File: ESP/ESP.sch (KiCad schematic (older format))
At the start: 28 parts, among them J3 USB_B_Micro, J4 Micro_SD_Card_Det, Q1 mmbt2222, Q2 mmbt2222, U1 ESP32-PICO-D4, U2 AP2112K-3.3, U3 CP2104

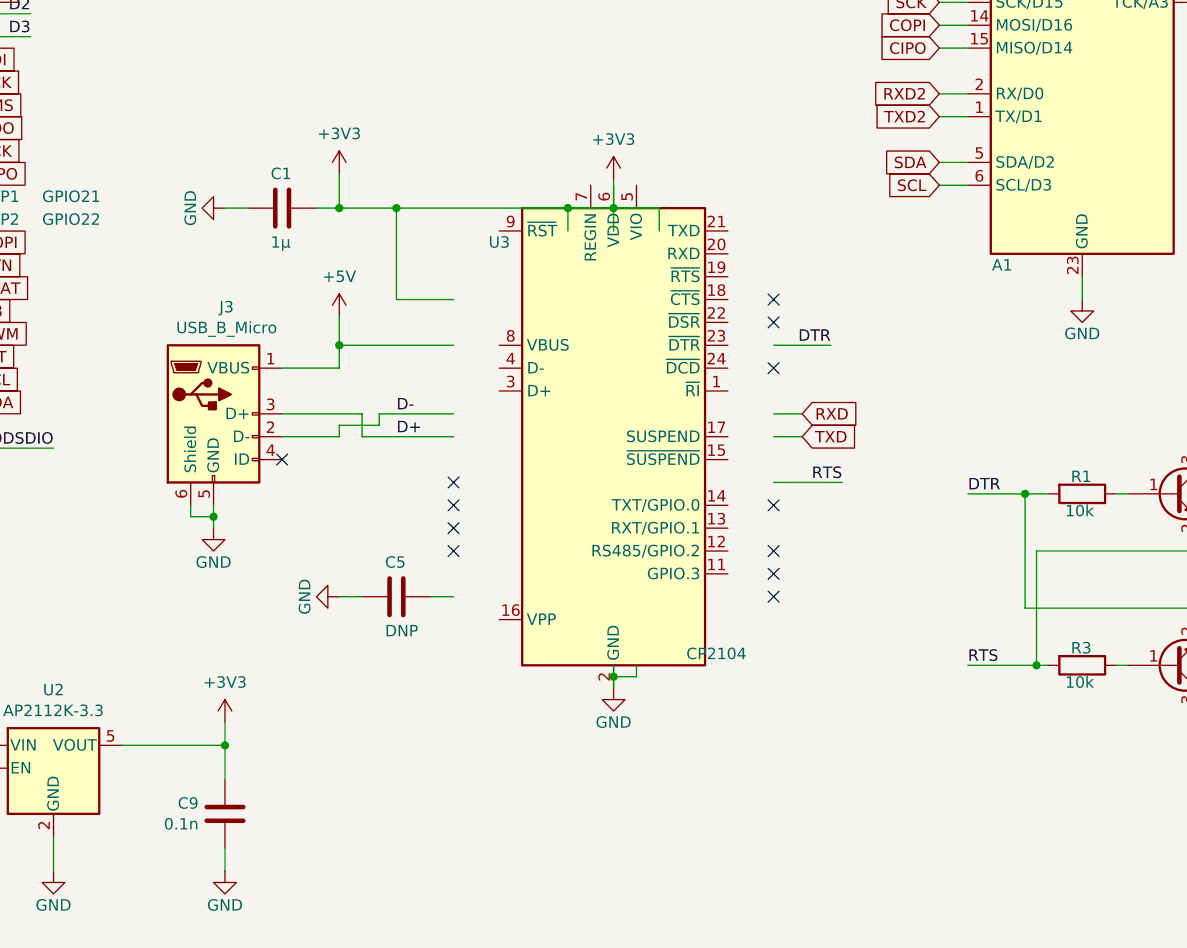
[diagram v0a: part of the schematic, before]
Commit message: changed VCC of CP2104
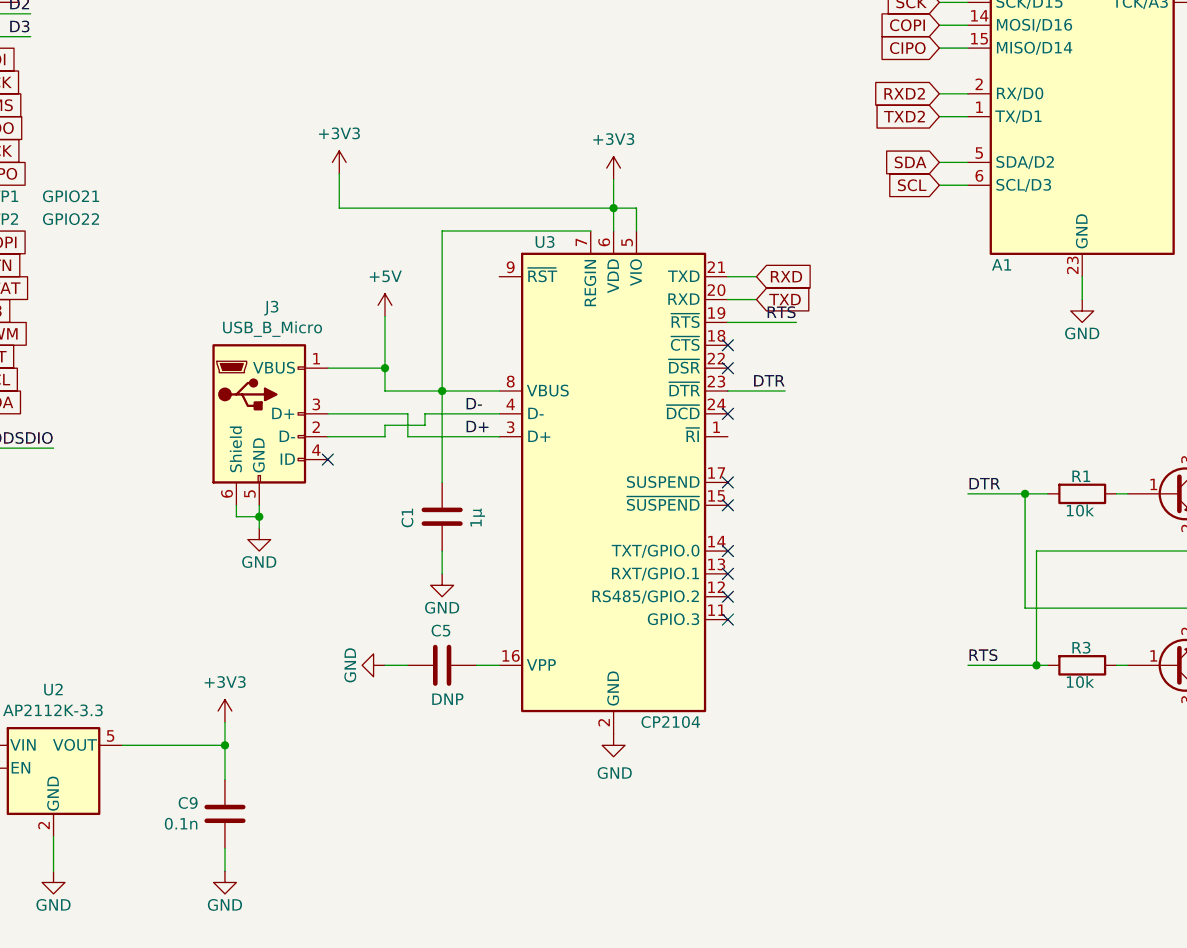
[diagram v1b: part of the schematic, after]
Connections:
- wire segments 160 -> 154
- no-connect marks 20 -> 18
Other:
- moved on the sheet: C1, C5, J3, U3
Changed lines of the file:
@@
 Sheet 1 1
 Title "ProMicro_ESP"
-Date "2021-04-19"
-Rev "v1.0"
+Date "2021-04-20"
+Rev "v1.1"
 Comp "nerdyscout"
 Comment1 ""
@@
 	9550 6000 9550 5500
 Connection ~ 9550 6000
-Wire Wire Line
-	9500 5250 9250 5250
 Connection ~ 9500 5250
 Wire Wire Line
@@
 $EndComp
 $Comp
-L power:GND #PWR0113
-U 1 1 60528891
-P 7700 6100
-F 0 "#PWR0113" H 7700 5850 50  0001 C CNN
-F 1 "GND" H 7700 5950 50  0000 C CNN
-F 2 "" H 7700 6100 50  0001 C CNN
-F 3 "" H 7700 6100 50  0001 C CNN
-	1    7700 6100
-	1    0    0    -1
-$EndComp
-Wire Wire Line
-	7700 6100 7700 6050
-Wire Wire Line
-	7700 6050 7800 6050
-Wire Wire Line
-	7800 6050 7800 6000
-Connection ~ 7700 6050
-Wire Wire Line
-	7700 6050 7700 6000
-$Comp
 L power:+3V3 #PWR0114
 U 1 1 60537586
@@
 Wire Wire Line
 	7700 4100 7700 4000
-Wire Wire Line
-	7500 4100 7500 4000
-Wire Wire Line
-	7500 4000 7700 4000
 Connection ~ 7700 4000
 Wire Wire Line
 	7700 4000 7700 3875
-Text GLabel 8525 5000 2    50   Input ~ 0
+Text GLabel 8325 4400 2    50   Input ~ 0
 TXD
-Text GLabel 8525 4900 2    50   Input ~ 0
+Text GLabel 8325 4300 2    50   Input ~ 0
 RXD
-Text Label 8650 4600 2    50   ~ 0
+Text Label 8450 4800 2    50   ~ 0
 DTR
-Text Label 8700 5200 2    50   ~ 0
+Text Label 8500 4500 2    50   ~ 0
 RTS
 Wire Wire Line
-	8400 5200 8700 5200
-Wire Wire Line
-	8400 4600 8650 4600
-Wire Wire Line
-	8525 5000 8400 5000
-Wire Wire Line
-	8400 4900 8525 4900
-NoConn ~ 8400 4400
-NoConn ~ 8400 4500
-NoConn ~ 8400 5300
+	8200 4500 8500 4500
+Wire Wire Line
+	8200 4800 8450 4800
+Wire Wire Line
+	8325 4400 8200 4400
+Wire Wire Line
+	8200 4300 8325 4300
+NoConn ~ 8200 4600
+NoConn ~ 8200 4700
+NoConn ~ 8200 5300
 $Comp
 L Device:C C1
 U 1 1 605A71B6
-P 6250 4000
-F 0 "C1" V 6100 3950 50  0000 L CNN
-F 1 "1µ" V 6400 3950 50  0000 L CNN
-F 2 "Capacitor_SMD:C_0603_1608Metric" H 6288 3850 50  0001 C CNN
-F 3 "~" H 6250 4000 50  0001 C CNN
-	1    6250 4000
-	0    1    1    0
-$EndComp
-Wire Wire Line
-	6400 4000 6500 4000
+P 6950 5350
+F 0 "C1" V 6800 5300 50  0000 L CNN
+F 1 "1µ" V 7100 5300 50  0000 L CNN
+F 2 "Capacitor_SMD:C_0603_1608Metric" H 6988 5200 50  0001 C CNN
+F 3 "~" H 6950 5350 50  0001 C CNN
+	1    6950 5350
+	1    0    0    -1
+$EndComp
 $Comp
 L power:GND #PWR0115
 U 1 1 605A71C1
-P 6000 4000
-F 0 "#PWR0115" H 6000 3750 50  0001 C CNN
-F 1 "GND" H 6000 3850 50  0000 C CNN
-F 2 "" H 6000 4000 50  0001 C CNN
-F 3 "" H 6000 4000 50  0001 C CNN
-	1    6000 4000
-	0    1    1    0
-$EndComp
-Wire Wire Line
-	6000 4000 6100 4000
+P 6950 5600
+F 0 "#PWR0115" H 6950 5350 50  0001 C CNN
+F 1 "GND" H 6950 5450 50  0000 C CNN
+F 2 "" H 6950 5600 50  0001 C CNN
+F 3 "" H 6950 5600 50  0001 C CNN
+	1    6950 5600
+	1    0    0    -1
+$EndComp
+Wire Wire Line
+	6950 5600 6950 5500
 $Comp
 L power:+3V3 #PWR0116
@@
 Wire Wire Line
 	6500 3850 6500 4000
-Connection ~ 6500 4000
-Wire Wire Line
-	6500 4000 6750 4000
-Connection ~ 7500 4000
-Wire Wire Line
-	7000 4400 6750 4400
-Wire Wire Line
-	7900 4100 7900 4000
-Wire Wire Line
-	7700 4000 7900 4000
-Wire Wire Line
-	6250 5000 6500 5000
-Wire Wire Line
-	6500 5000 6500 4950
-Wire Wire Line
-	6500 4950 6675 4950
-Wire Wire Line
-	6675 4950 6675 4900
-Wire Wire Line
-	6675 4900 7000 4900
-Wire Wire Line
-	7000 5000 6600 5000
-Wire Wire Line
-	6600 5000 6600 4900
-Wire Wire Line
-	6600 4900 6250 4900
+Wire Wire Line
+	7700 4000 7800 4000
+Wire Wire Line
+	6450 5000 6700 5000
+Wire Wire Line
+	6700 5000 6700 4950
+Wire Wire Line
+	6700 4950 6875 4950
+Wire Wire Line
+	6875 4950 6875 4900
+Wire Wire Line
+	6875 4900 7200 4900
+Wire Wire Line
+	7200 5000 6800 5000
+Wire Wire Line
+	6800 5000 6800 4900
+Wire Wire Line
+	6800 4900 6450 4900
 $Comp
 L power:GND #PWR0118
 U 1 1 6060CE03
-P 5950 5400
-F 0 "#PWR0118" H 5950 5150 50  0001 C CNN
-F 1 "GND" H 5950 5250 50  0000 C CNN
-F 2 "" H 5950 5400 50  0001 C CNN
-F 3 "" H 5950 5400 50  0001 C CNN
-	1    5950 5400
-	1    0    0    -1
-$EndComp
-Wire Wire Line
-	5950 5400 5950 5350
-Wire Wire Line
-	5950 5350 5850 5350
-Wire Wire Line
-	5850 5350 5850 5300
-Connection ~ 5950 5350
-Wire Wire Line
-	5950 5350 5950 5300
+P 6150 5400
+F 0 "#PWR0118" H 6150 5150 50  0001 C CNN
+F 1 "GND" H 6150 5250 50  0000 C CNN
+F 2 "" H 6150 5400 50  0001 C CNN
+F 3 "" H 6150 5400 50  0001 C CNN
+	1    6150 5400
+	1    0    0    -1
+$EndComp
+Wire Wire Line
+	6150 5400 6150 5350
+Wire Wire Line
+	6150 5350 6050 5350
+Wire Wire Line
+	6050 5350 6050 5300
+Connection ~ 6150 5350
+Wire Wire Line
+	6150 5350 6150 5300
 Text Label 3150 6600 2    50   ~ 0
 CLK
@@
 L power:+5V #PWR0126
 U 1 1 60613DA0
-P 6500 4475
-F 0 "#PWR0126" H 6500 4325 50  0001 C CNN
-F 1 "+5V" H 6500 4650 50  0000 C CNN
-F 2 "" H 6500 4475 50  0001 C CNN
-F 3 "" H 6500 4475 50  0001 C CNN
-	1    6500 4475
-	1    0    0    -1
-$EndComp
-Wire Wire Line
-	7000 4600 6500 4600
-Wire Wire Line
-	6500 4600 6500 4475
-Wire Wire Line
-	6250 4700 6500 4700
-Wire Wire Line
-	6500 4700 6500 4600
-Connection ~ 6500 4600
-Wire Wire Line
-	6750 4400 6750 4000
-Connection ~ 6750 4000
-Wire Wire Line
-	6750 4000 7500 4000
+P 6700 4475
+F 0 "#PWR0126" H 6700 4325 50  0001 C CNN
+F 1 "+5V" H 6700 4650 50  0000 C CNN
+F 2 "" H 6700 4475 50  0001 C CNN
+F 3 "" H 6700 4475 50  0001 C CNN
+	1    6700 4475
+	1    0    0    -1
+$EndComp
+Wire Wire Line
+	6450 4700 6700 4700
 $Comp
 L Regulator_Linear:AP2112K-3.3 U2
@@
 L Connector:USB_B_Micro J3
 U 1 1 6079D873
-P 5950 4900
-F 0 "J3" H 6007 5367 50  0000 C CNN
-F 1 "USB_B_Micro" H 6007 5276 50  0000 C CNN
-F 2 "Connector_USB:USB_Micro-B_Molex_47346-0001" H 6100 4850 50  0001 C CNN
-F 3 "~" H 6100 4850 50  0001 C CNN
-	1    5950 4900
+P 6150 4900
+F 0 "J3" H 6207 5367 50  0000 C CNN
+F 1 "USB_B_Micro" H 6207 5276 50  0000 C CNN
+F 2 "Connector_USB:USB_Micro-B_Molex_47346-0001" H 6300 4850 50  0001 C CNN
+F 3 "~" H 6300 4850 50  0001 C CNN
+	1    6150 4900
 	1    0    0    -1
 $EndComp
@@
 L Interface_USB:CP2104 U3
 U 1 1 604CC18C
-P 7700 5000
-F 0 "U3" H 7200 5850 50  0000 C CNN
-F 1 "CP2104" H 8150 4050 50  0000 C CNN
-F 2 "Package_DFN_QFN:QFN-24-1EP_4x4mm_P0.5mm_EP2.6x2.6mm" H 7850 4050 50  0001 L CNN
-F 3 "https://www.silabs.com/documents/public/data-sheets/cp2104.pdf" H 7150 6250 50  0001 C CNN
-	1    7700 5000
-	1    0    0    -1
-$EndComp
-Wire Wire Line
-	6900 5700 7000 5700
+P 7700 5200
+F 0 "U3" H 7400 6250 50  0000 C CNN
+F 1 "CP2104" H 7950 4150 50  0000 C CNN
+F 2 "Package_DFN_QFN:QFN-24-1EP_4x4mm_P0.5mm_EP2.6x2.6mm" H 7850 4250 50  0001 L CNN
+F 3 "https://www.silabs.com/documents/public/data-sheets/cp2104.pdf" H 7150 6450 50  0001 C CNN
+	1    7700 5200
+	1    0    0    -1
+$EndComp
+Wire Wire Line
+	7100 6000 7200 6000
 $Comp
 L Device:C C5
 U 1 1 60643A1C
-P 6750 5700
-F 0 "C5" V 6600 5650 50  0000 L CNN
-F 1 "DNP" V 6900 5650 50  0000 L CNN
-F 2 "Capacitor_SMD:C_0603_1608Metric" H 6788 5550 50  0001 C CNN
-F 3 "~" H 6750 5700 50  0001 C CNN
-	1    6750 5700
+P 6950 6000
+F 0 "C5" V 6800 5950 50  0000 L CNN
+F 1 "DNP" V 7100 5950 50  0000 L CNN
+F 2 "Capacitor_SMD:C_0603_1608Metric" H 6988 5850 50  0001 C CNN
+F 3 "~" H 6950 6000 50  0001 C CNN
+	1    6950 6000
 	0    1    1    0
 $EndComp
@@
 L power:GND #PWR0122
 U 1 1 60643A27
-P 6500 5700
-F 0 "#PWR0122" H 6500 5450 50  0001 C CNN
-F 1 "GND" H 6500 5550 50  0000 C CNN
-F 2 "" H 6500 5700 50  0001 C CNN
-F 3 "" H 6500 5700 50  0001 C CNN
-	1    6500 5700
+P 6700 6000
+F 0 "#PWR0122" H 6700 5750 50  0001 C CNN
+F 1 "GND" H 6700 5850 50  0000 C CNN
+F 2 "" H 6700 6000 50  0001 C CNN
+F 3 "" H 6700 6000 50  0001 C CNN
+	1    6700 6000
 	0    1    1    0
 $EndComp
 Wire Wire Line
-	6500 5700 6600 5700
+	6700 6000 6800 6000
 Wire Wire Line
 	3225 6200 2750 6200
@@
 Text GLabel 3650 6200 2    50   Input ~ 0
 BTN
-Text Label 6750 4900 0    50   ~ 0
+Text Label 7050 4900 0    50   ~ 0
 D-
-Text Label 6750 5000 0    50   ~ 0
+Text Label 7050 5000 0    50   ~ 0
 D+
 $Comp
@@
 	1    0    0    -1
 $EndComp
-NoConn ~ 8400 5700
-NoConn ~ 8400 5600
-NoConn ~ 8400 5500
-NoConn ~ 7000 5500
-NoConn ~ 7000 5400
-NoConn ~ 7000 5300
-NoConn ~ 7000 5200
-NoConn ~ 8400 4700
-NoConn ~ 6250 5100
+NoConn ~ 8200 4900
+NoConn ~ 6450 5100
 Wire Wire Line
 	2750 4250 3150 4250
 Text Label 2750 4250 0    50   ~ 0
 CMD
+Wire Wire Line
+	7800 4100 7800 4000
+Wire Wire Line
+	9250 5250 9500 5250
+NoConn ~ 8200 5500
+NoConn ~ 8200 5600
+NoConn ~ 8200 5700
+NoConn ~ 8200 5800
+NoConn ~ 8200 5200
+Wire Wire Line
+	7200 4800 6950 4800
+Wire Wire Line
+	6700 4800 6700 4700
+Connection ~ 6700 4700
+Wire Wire Line
+	6700 4475 6700 4700
+$Comp
+L power:GND #PWR?
+U 1 1 608A027A
+P 7700 6300
+F 0 "#PWR?" H 7700 6050 50  0001 C CNN
+F 1 "GND" H 7705 6127 50  0000 C CNN
+F 2 "" H 7700 6300 50  0001 C CNN
+F 3 "" H 7700 6300 50  0001 C CNN
+	1    7700 6300
+	1    0    0    -1
+$EndComp
+Wire Wire Line
+	6500 4000 7700 4000
+Wire Wire Line
+	7600 4100 6950 4100
+Wire Wire Line
+	6950 4100 6950 4800
+Connection ~ 6950 4800
+Wire Wire Line
+	6950 4800 6700 4800
+Wire Wire Line
+	6950 4800 6950 5200
 $EndSCHEMATC

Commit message: blindly dumped everything
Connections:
- no-connect marks 18 -> 19
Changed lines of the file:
@@
 encoding utf-8
 Sheet 1 1
-Title "ProMicro_ESP"
+Title "ESP"
 Date "2021-04-20"
 Rev "v1.1"
@@
 Wire Wire Line
 	6950 5600 6950 5500
-$Comp
-L power:+3V3 #PWR0116
-U 1 1 605A71CC
-P 6500 3850
-F 0 "#PWR0116" H 6500 3700 50  0001 C CNN
-F 1 "+3V3" H 6500 4025 50  0000 C CNN
-F 2 "" H 6500 3850 50  0001 C CNN
-F 3 "" H 6500 3850 50  0001 C CNN
-	1    6500 3850
-	1    0    0    -1
-$EndComp
-Wire Wire Line
-	6500 3850 6500 4000
 Wire Wire Line
 	7700 4000 7800 4000
@@
 L power:+5V #PWR0126
 U 1 1 60613DA0
-P 6700 4475
-F 0 "#PWR0126" H 6700 4325 50  0001 C CNN
-F 1 "+5V" H 6700 4650 50  0000 C CNN
-F 2 "" H 6700 4475 50  0001 C CNN
-F 3 "" H 6700 4475 50  0001 C CNN
-	1    6700 4475
+P 6950 3875
+F 0 "#PWR0126" H 6950 3725 50  0001 C CNN
+F 1 "+5V" H 6950 4050 50  0000 C CNN
+F 2 "" H 6950 3875 50  0001 C CNN
+F 3 "" H 6950 3875 50  0001 C CNN
+	1    6950 3875
 	1    0    0    -1
 $EndComp
@@
 Wire Wire Line
 	6700 4800 6700 4700
-Connection ~ 6700 4700
-Wire Wire Line
-	6700 4475 6700 4700
-$Comp
-L power:GND #PWR?
+Wire Wire Line
+	6950 3875 6950 4100
+$Comp
+L power:GND #PWR0105
 U 1 1 608A027A
 P 7700 6300
-F 0 "#PWR?" H 7700 6050 50  0001 C CNN
+F 0 "#PWR0105" H 7700 6050 50  0001 C CNN
 F 1 "GND" H 7705 6127 50  0000 C CNN
 F 2 "" H 7700 6300 50  0001 C CNN
@@
 $EndComp
 Wire Wire Line
-	6500 4000 7700 4000
-Wire Wire Line
 	7600 4100 6950 4100
 Wire Wire Line
@@
 Wire Wire Line
 	6950 4800 6950 5200
+NoConn ~ 8200 5000
+Connection ~ 6950 4100
 $EndSCHEMATC
